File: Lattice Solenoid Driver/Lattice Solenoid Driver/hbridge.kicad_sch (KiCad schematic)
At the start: 9 parts, among them J1 Conn_01x05_Pin, U3 DRV8873SPWPR

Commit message: Finished Rev 1 initial
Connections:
- net GND: now also U3.EPAD; no longer U3.25 (EPAD)
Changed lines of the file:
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@@
     (pin "23")
     (pin "24")
-    (pin "25")
+    (pin "EPAD")
     (pin "3")
     (pin "4")

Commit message: finishing touches
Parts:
- U3: Part # (none) -> C2150662
- renumbered C7 to C4, C11 to C5, C15 to C6, C19 to C7, C23 to C8, C27 to C9, J1 to J3

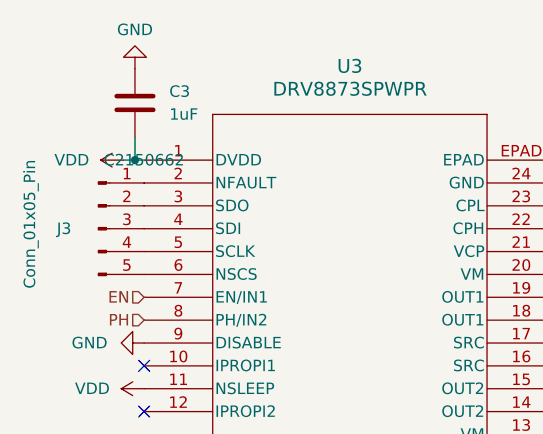
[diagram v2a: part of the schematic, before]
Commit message: adding stepper driver
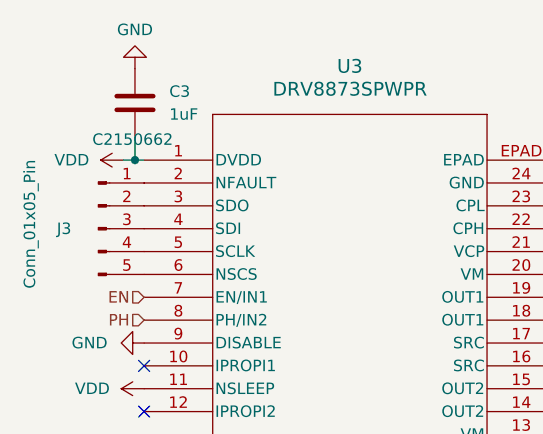
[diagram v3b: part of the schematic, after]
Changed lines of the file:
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@@
 		(on_board yes)
 		(dnp no)
-		(fields_autoplaced yes)
 		(property "Reference" "U3"
 			(at 144.78 75.184 0)
@@
 		)
 		(property "Part #" "C2150662"
-			(at 121.92 85.598 0)
+			(at 120.65 83.312 0)
 			(effects
 				(font
